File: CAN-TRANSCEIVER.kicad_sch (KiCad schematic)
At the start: 0 parts

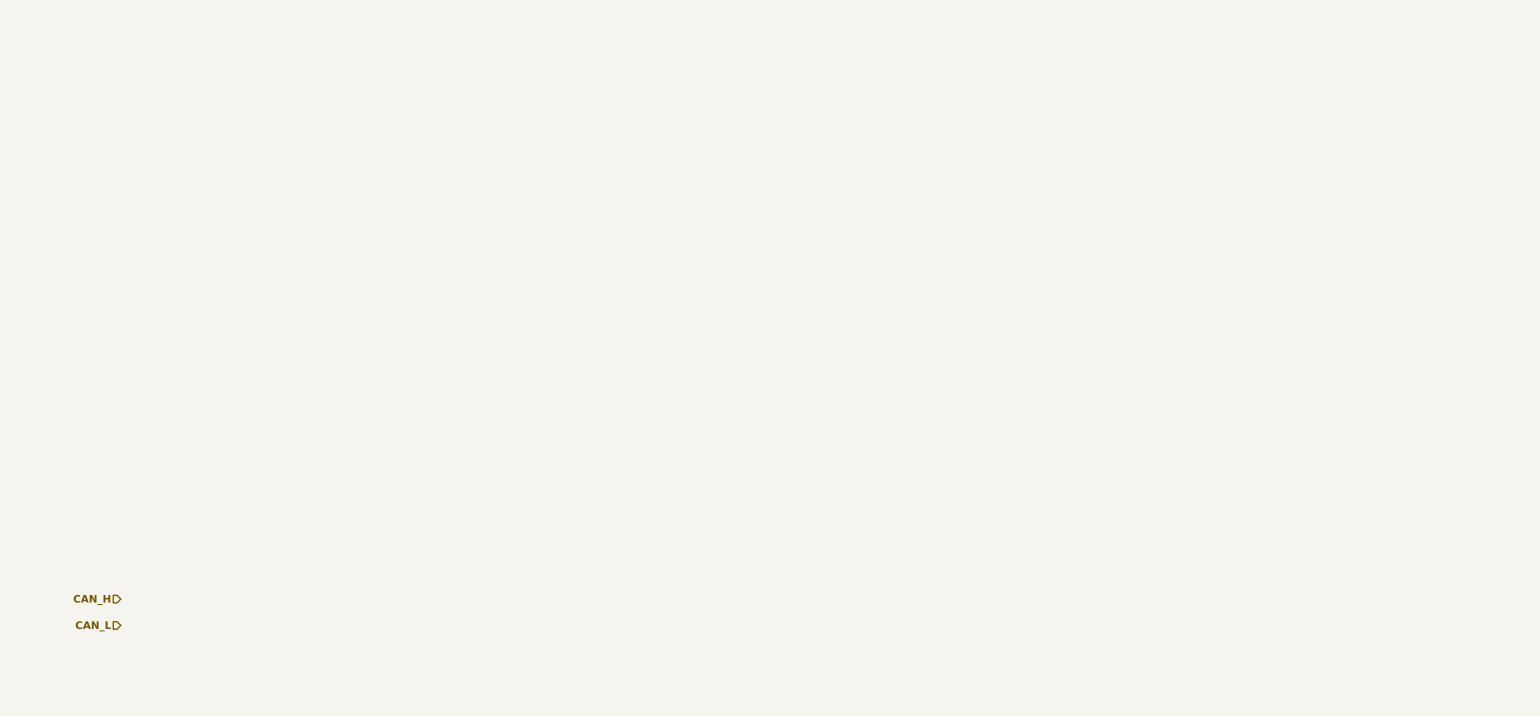
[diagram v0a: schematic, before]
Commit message: Added CAN Transceiver
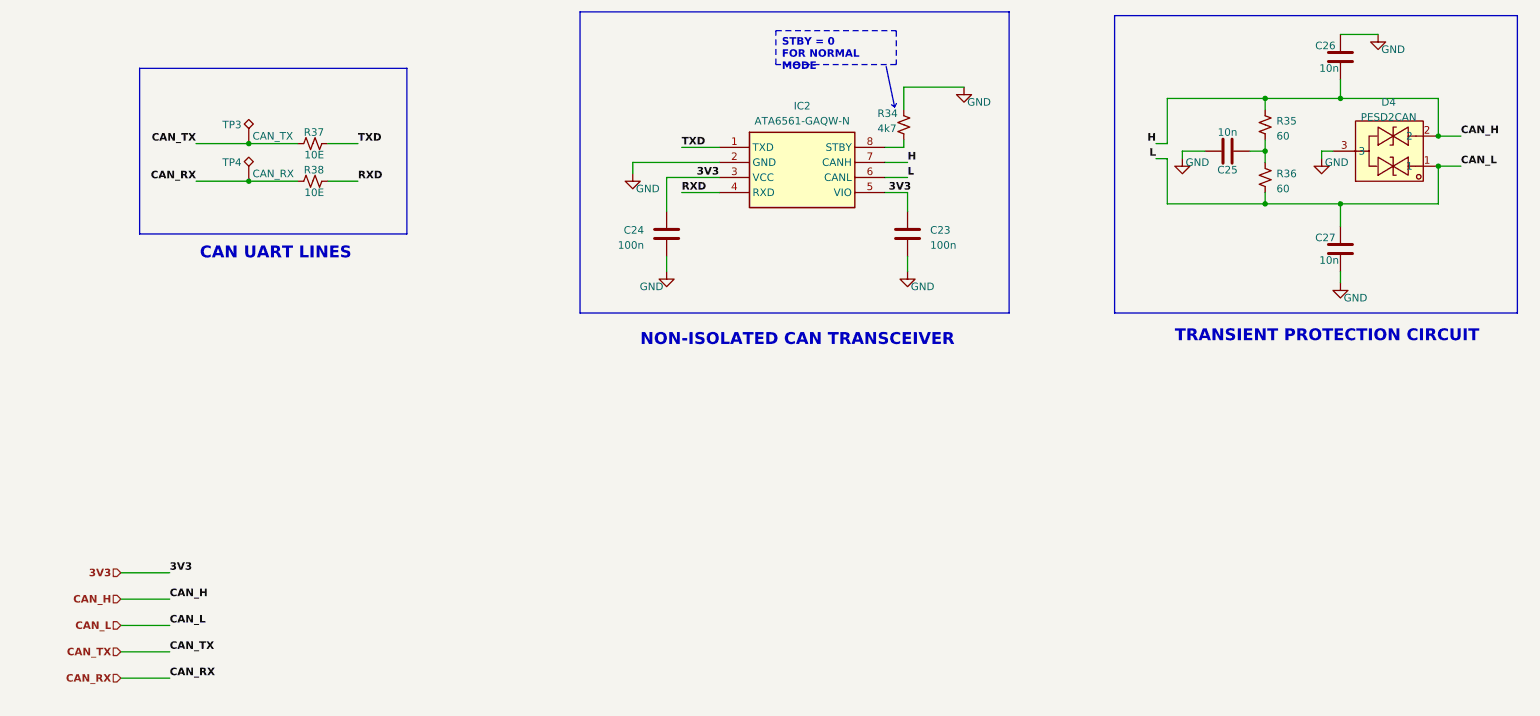
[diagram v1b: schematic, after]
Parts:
- added C23, C24: 100n, symbol ESP32-S3_DB:C
- added C25, C26, C27: 10n, symbol ESP32-S3_DB:C
- added D4: PESD2CAN, easyeda2kicad:SOT-23-3_L2.9-W1.3-P1.90-LS2.4-BR, symbol ESP32-S3_DB:PESD2CAN
- added IC2: ATA6561-GAQW-N, SOIC127P600X175-8N, symbol ESP32-S3_DB:ATA6561-GAQW-N
- added R34: 4k7, symbol ESP32-S3_DB:R_Small_US
- added R35, R36: 60, symbol ESP32-S3_DB:R_Small_US
- added R37, R38: 10E, symbol ESP32-S3_DB:R_Small_US
- added TP3: CAN_TX, symbol ESP32-S3_DB:TestPoint_Alt
- added TP4: CAN_RX, symbol ESP32-S3_DB:TestPoint_Alt
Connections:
- net CAN_H: now also C26.1, D4.2, IC2.7 (CANH), R35.2
- net CAN_L: now also C27.2, D4.1, IC2.6 (CANL), R36.1
- new net: IC2.8 (STBY), R34.1
- new net: C25.2, R35.1, R36.2
- new net 3V3: C23.1, C24.2, IC2.3 (VCC), IC2.5 (VIO)
- new net CAN_RX: R38.2, TP4.1
- new net CAN_TX: R37.2, TP3.1
- new net GND: C23.2, C24.1, C25.1, C26.2, C27.1, D4.3, IC2.2 (GND), R34.2
- new net RXD: IC2.4 (RXD), R38.1
- new net TXD: IC2.1 (TXD), R37.1
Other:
- note added: "CAN UART LINES"
- note added: "NON-ISOLATED CAN TRANSCEIVER"
- note added: "TRANSIENT PROTECTION CIRCUIT"

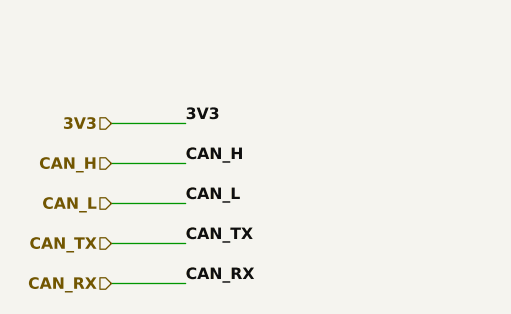
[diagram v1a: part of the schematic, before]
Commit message: Added IP5306 for power path management
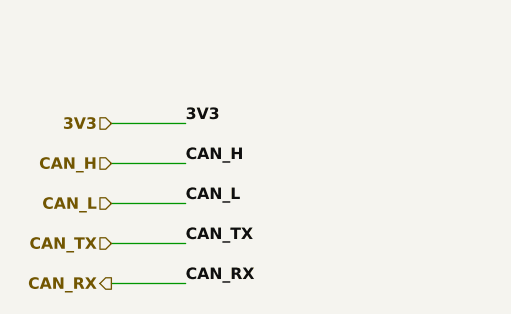
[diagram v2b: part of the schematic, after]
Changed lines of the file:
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@@
     (effects (font (size 1.27 1.27) bold (color 0 0 0 1)) (justify right))
   )
-  (hierarchical_label "CAN_RX" (shape input) (at 33.655 185.42 180) (fields_autoplaced)
+  (hierarchical_label "CAN_RX" (shape output) (at 33.655 185.42 180) (fields_autoplaced)
     (effects (font (size 1.27 1.27) bold (color 0 0 255 1)) (justify right))
   )

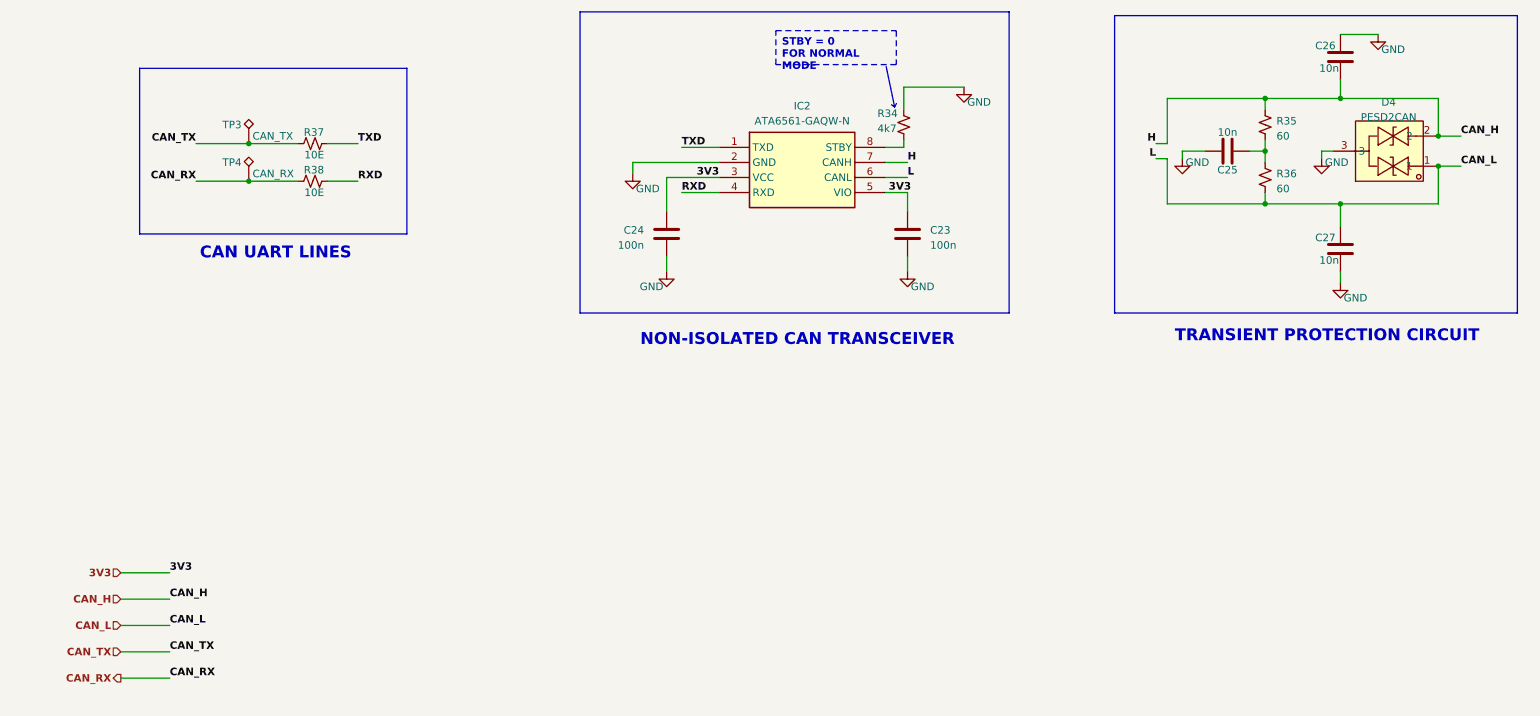
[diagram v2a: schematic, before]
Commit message: Added Female Headers
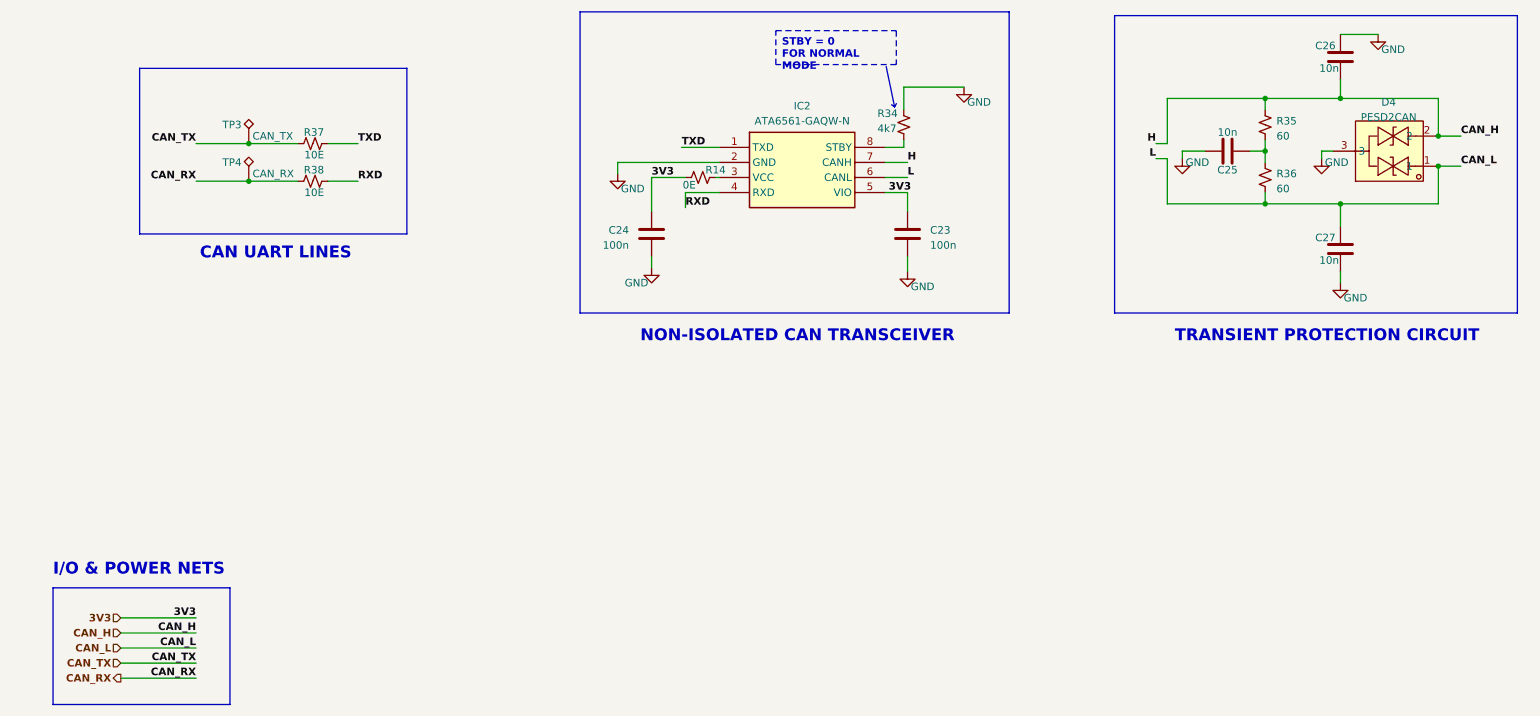
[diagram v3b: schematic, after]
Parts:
- added R14: 0E, symbol ESP32-S3_DB:R_Small_US
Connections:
- net 3V3: now also R14.1; no longer IC2.3 (VCC)
- new net: IC2.3 (VCC), R14.2
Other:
- note added: "I/O & POWER NETS"
- moved on the sheet: C24

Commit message: Assigned PN and Footprint for C
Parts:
- C23, C24: value 100n -> 100nF; footprint (none) -> ESP32-S3_DB:C_0402_1005Metric; PN (none) -> EMK107B7104KAHT
- C25, C26, C27: value 10n -> 10nF; footprint (none) -> ESP32-S3_DB:C_0402_1005Metric; PN (none) -> CC0402KRX7R9BB103
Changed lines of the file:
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@@
       (effects (font (size 1.27 1.27)) (justify left))
     )
-    (property "Value" "100n" (at 170.18 112.395 0)
+    (property "Value" "100nF" (at 170.18 112.395 0)
       (effects (font (size 1.27 1.27)) (justify left))
     )
-    (property "Footprint" "" (at 167.3352 114.3 0)
+    (property "Footprint" "ESP32-S3_DB:C_0402_1005Metric" (at 167.3352 114.3 0)
       (effects (font (size 1.27 1.27)) hide)
     )
@@
       (effects (font (size 1.27 1.27)) hide)
     )
+    (property "PN" "EMK107B7104KAHT" (at 166.37 110.49 0)
+      (effects (font (size 1.27 1.27)) hide)
+    )
     (pin "1")
     (pin "2")
@@
       (effects (font (size 1.27 1.27)) (justify right))
     )
-    (property "Value" "100n" (at 119.38 112.395 0)
-      (effects (font (size 1.27 1.27)) (justify right))
-    )
-    (property "Footprint" "" (at 124.1552 106.68 0)
+    (property "Value" "100nF" (at 119.38 112.395 0)
+      (effects (font (size 1.27 1.27)) (justify right))
+    )
+    (property "Footprint" "ESP32-S3_DB:C_0402_1005Metric" (at 124.1552 106.68 0)
       (effects (font (size 1.27 1.27)) hide)
     )
     (property "Datasheet" "~" (at 123.19 110.49 0)
+      (effects (font (size 1.27 1.27)) hide)
+    )
+    (property "PN" "EMK107B7104KAHT" (at 123.19 110.49 0)
       (effects (font (size 1.27 1.27)) hide)
     )
@@
       (effects (font (size 1.27 1.27)))
     )
-    (property "Value" "10n" (at 237.49 82.55 0)
-      (effects (font (size 1.27 1.27)))
-    )
-    (property "Footprint" "" (at 238.4298 76.835 0)
+    (property "Value" "10nF" (at 237.49 82.55 0)
+      (effects (font (size 1.27 1.27)))
+    )
+    (property "Footprint" "ESP32-S3_DB:C_0402_1005Metric" (at 238.4298 76.835 0)
       (effects (font (size 1.27 1.27)) hide)
     )
     (property "Datasheet" "~" (at 239.395 80.645 0)
+      (effects (font (size 1.27 1.27)) hide)
+    )
+    (property "PN" "CC0402KRX7R9BB103" (at 239.395 80.645 0)
       (effects (font (size 1.27 1.27)) hide)
     )
@@
       (effects (font (size 1.27 1.27)))
     )
-    (property "Value" "10n" (at 220.345 93.345 90)
-      (effects (font (size 1.27 1.27)))
-    )
-    (property "Footprint" "" (at 224.155 95.5548 0)
+    (property "Value" "10nF" (at 220.345 93.345 90)
+      (effects (font (size 1.27 1.27)))
+    )
+    (property "Footprint" "ESP32-S3_DB:C_0402_1005Metric" (at 224.155 95.5548 0)
       (effects (font (size 1.27 1.27)) hide)
     )
@@
       (effects (font (size 1.27 1.27)) hide)
     )
+    (property "PN" "CC0402KRX7R9BB103" (at 220.345 96.52 0)
+      (effects (font (size 1.27 1.27)) hide)
+    )
     (pin "1")
     (pin "2")
@@
       (effects (font (size 1.27 1.27)))
     )
-    (property "Value" "10n" (at 237.49 114.935 0)
-      (effects (font (size 1.27 1.27)))
-    )
-    (property "Footprint" "" (at 238.4298 109.22 0)
+    (property "Value" "10nF" (at 237.49 114.935 0)
+      (effects (font (size 1.27 1.27)))
+    )
+    (property "Footprint" "ESP32-S3_DB:C_0402_1005Metric" (at 238.4298 109.22 0)
       (effects (font (size 1.27 1.27)) hide)
     )
@@
       (effects (font (size 1.27 1.27)) hide)
     )
+    (property "PN" "CC0402KRX7R9BB103" (at 239.395 113.03 0)
+      (effects (font (size 1.27 1.27)) hide)
+    )
